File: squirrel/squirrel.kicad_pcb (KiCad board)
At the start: 2 copper layers, 170 x 152 mm, 69 parts, among them J1 Conn_01x01, J10 Conn_01x01, J11 Conn_01x01, J12 Conn_01x01, J13 Conn_01x01, J14 Conn_01x01, J15 Conn_01x01, J16 Conn_01x01, J17 Conn_01x01, J18 Conn_01x01, J19 Conn_01x01, J2 Conn_01x01, J20 Conn_01x01, J21 Conn_01x01, J22 Conn_01x01, J23 Conn_01x01, J24 Conn_01x01, J25 Conn_01x01, J26 Conn_01x01, J27 Conn_01x01, J28 Conn_01x01, J29 Conn_01x01, J3 Conn_01x01, J30 Conn_01x01, J31 Conn_01x01, J32 Conn_01x01, J33 Conn_01x01, J34 Conn_01x01, J35 Conn_01x01, J36 Conn_01x01, J37 Conn_01x01, J38 Conn_01x01, J39 Conn_01x01, J4 Conn_01x01, J40 Conn_01x01, J41 Conn_02x20_Odd_Even, J42 Conn_01x02, J43 Conn_02x20_Odd_Even, J44 Conn_02x25_Odd_Even, J5 Conn_01x01, J6 Conn_01x01, J7 Conn_01x01, J8 Conn_01x01, J9 Conn_01x01

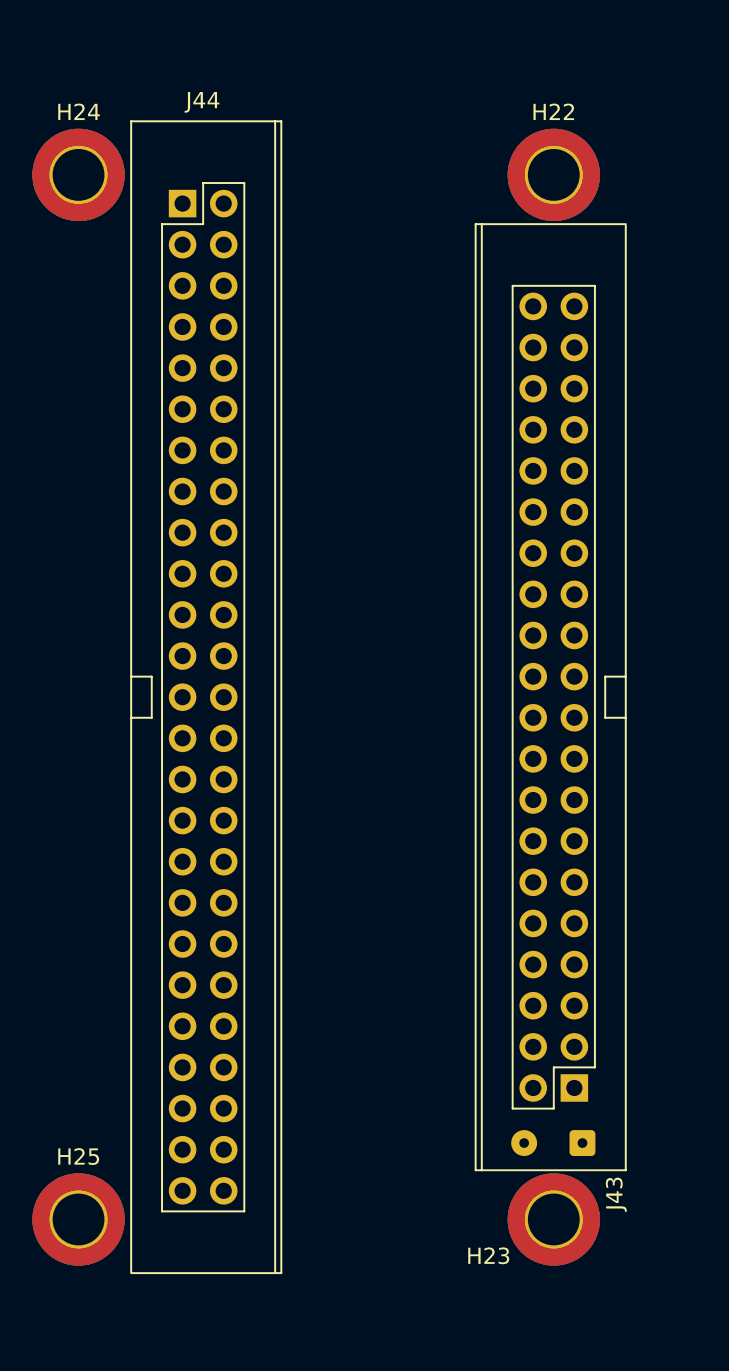
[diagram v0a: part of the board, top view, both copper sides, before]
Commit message: smaller pt pcb
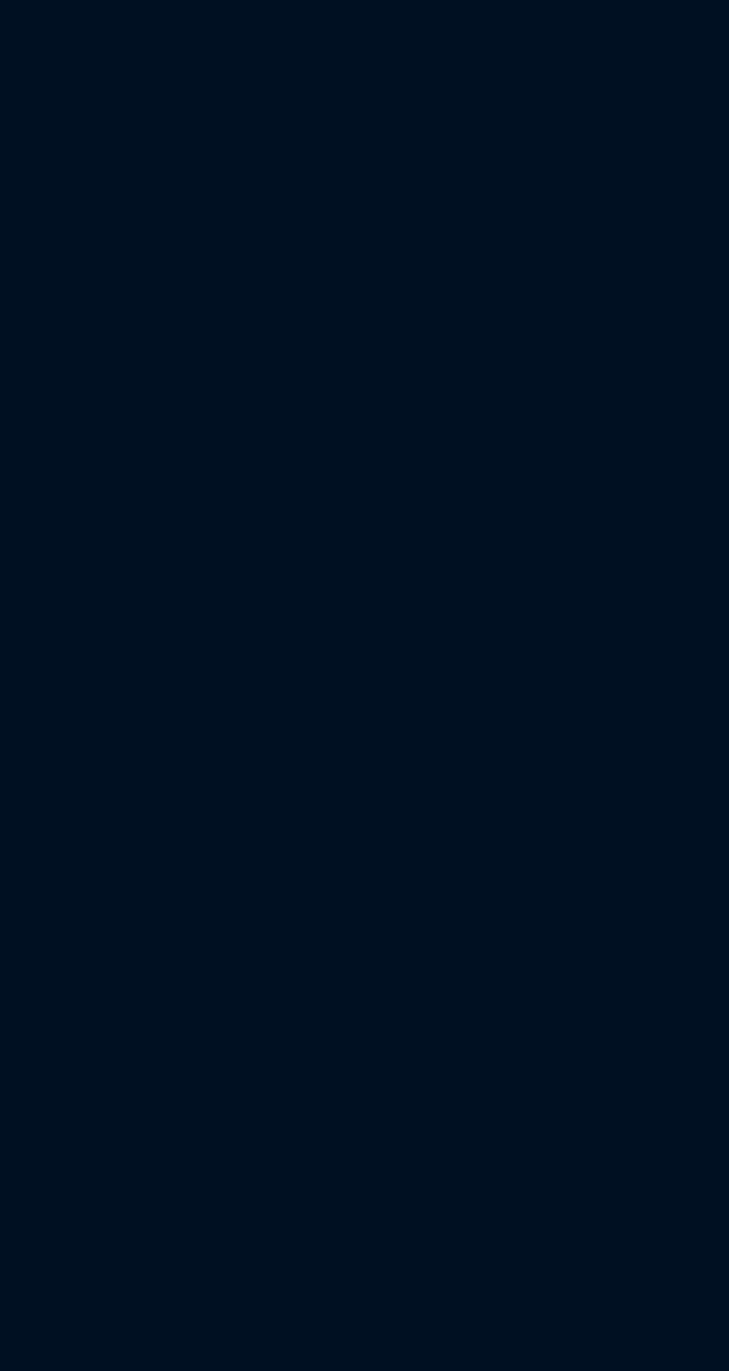
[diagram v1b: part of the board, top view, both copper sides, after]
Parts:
- removed H22, H23, H24, H25: MountingHole_Pad, custom_footprints:MountingHole_3.2mm_M3_ISO7380_Pad_TopBottom_screw
- removed J42: Conn_01x02, Connector_Wire:SolderWire-0.1sqmm_1x02_P3.6mm_D0.4mm_OD1mm
- removed J43: Conn_02x20_Odd_Even, custom_footprints:TST-120-01-G-D
- removed J44: Conn_02x25_Odd_Even, custom_footprints:TST-125-01-G-D

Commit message: sqpcbs layed out
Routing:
- net /S17: track 0.00 -> 216.8 mm
- net /F17: track 0.00 -> 215.1 mm
- net /F13: track 0.00 -> 199.6 mm
- net /S13: track 0.00 -> 197.7 mm
- net /F9: track 0.00 -> 182.1 mm
- net /S9: track 0.00 -> 180.0 mm
- net /S18: track 0.00 -> 178.4 mm
- net /F18: track 0.00 -> 177.5 mm
- net /S1: track 0.00 -> 176.6 mm
- net /F1: track 0.00 -> 167.9 mm
- net /S5: track 0.00 -> 167.4 mm
- net /F5: track 0.00 -> 165.6 mm
- net /F14: track 0.00 -> 161.7 mm
- net /S14: track 0.00 -> 161.1 mm
- net /S19: track 0.00 -> 154.1 mm
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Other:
- copper layers 2 -> 4

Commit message: silk
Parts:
- added LOGO1: Logo_Open_Hardware_Small, custom_footprints:site_small, B.Cu at (79.0, 0.00)
- added LOGO2: Logo_Open_Hardware_Small, custom_footprints:site_small, B.Cu at (-85.1, 46.9)
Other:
- board text added: "2736463"

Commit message: update silk
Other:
- board text added: "f74efd5"
- board text removed: "2736463"
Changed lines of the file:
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@@
   (gr_arc (start 19.5 37.5) (mid 20.207107 37.792893) (end 20.5 38.5) (layer "Edge.Cuts") (width 0.1))
   (gr_line (start -47.5 41.677) (end -41.823 41.677) (layer "Edge.Cuts") (width 0.1))
-  (gr_text "2736463" (at -87.3 40.4 -90) (layer "B.SilkS")
+  (gr_text "f74efd5" (at -87 40 -90) (layer "B.SilkS")
     (effects (font (size 1 1) (thickness 0.15)) (justify mirror))
   )
+  (gr_text "f74efd5" (at -87.015256 39.999999 -90) (layer "F.SilkS")
+    (effects (font (size 1 1) (thickness 0.15)))
+  )
   (segment (start -71.3 -44.7) (end -78.11 -51.51) (width 0.4) (layer "In1.Cu") (net 1))

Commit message: add dummy copper
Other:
- board text added: "COPPER BOT"
- board text added: "COPPER TOP"
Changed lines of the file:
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@@
       (outputformat 1)
       (mirror false)
-      (drillshape 1)
+      (drillshape 0)
       (scaleselection 1)
-      (outputdirectory "")
+      (outputdirectory "output/")
     )
   )
@@
   (gr_arc (start 19.5 37.5) (mid 20.207107 37.792893) (end 20.5 38.5) (layer "Edge.Cuts") (width 0.1))
   (gr_line (start -47.5 41.677) (end -41.823 41.677) (layer "Edge.Cuts") (width 0.1))
+  (gr_text "COPPER TOP" (at -86 12 90) (layer "F.Cu")
+    (effects (font (size 1.5 1.5) (thickness 0.3)))
+  )
+  (gr_text "COPPER BOT" (at -86 28 90) (layer "B.Cu")
+    (effects (font (size 1.5 1.5) (thickness 0.3)) (justify mirror))
+  )
   (gr_text "f74efd5" (at -87 40 -90) (layer "B.SilkS")
     (effects (font (size 1 1) (thickness 0.15)) (justify mirror))

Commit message: update silk
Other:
- board text added: "050ec02"
- board text removed: "f74efd5"
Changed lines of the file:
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@@
     (effects (font (size 1.5 1.5) (thickness 0.3)) (justify mirror))
   )
-  (gr_text "f74efd5" (at -87 40 -90) (layer "B.SilkS")
+  (gr_text "050ec02" (at -87 40 -90) (layer "B.SilkS")
     (effects (font (size 1 1) (thickness 0.15)) (justify mirror))
   )
-  (gr_text "f74efd5" (at -87.015256 39.999999 -90) (layer "F.SilkS")
+  (gr_text "050ec02" (at -87.015256 39.999999 -90) (layer "F.SilkS")
     (effects (font (size 1 1) (thickness 0.15)))
   )
